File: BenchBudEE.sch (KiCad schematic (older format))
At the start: 0 parts

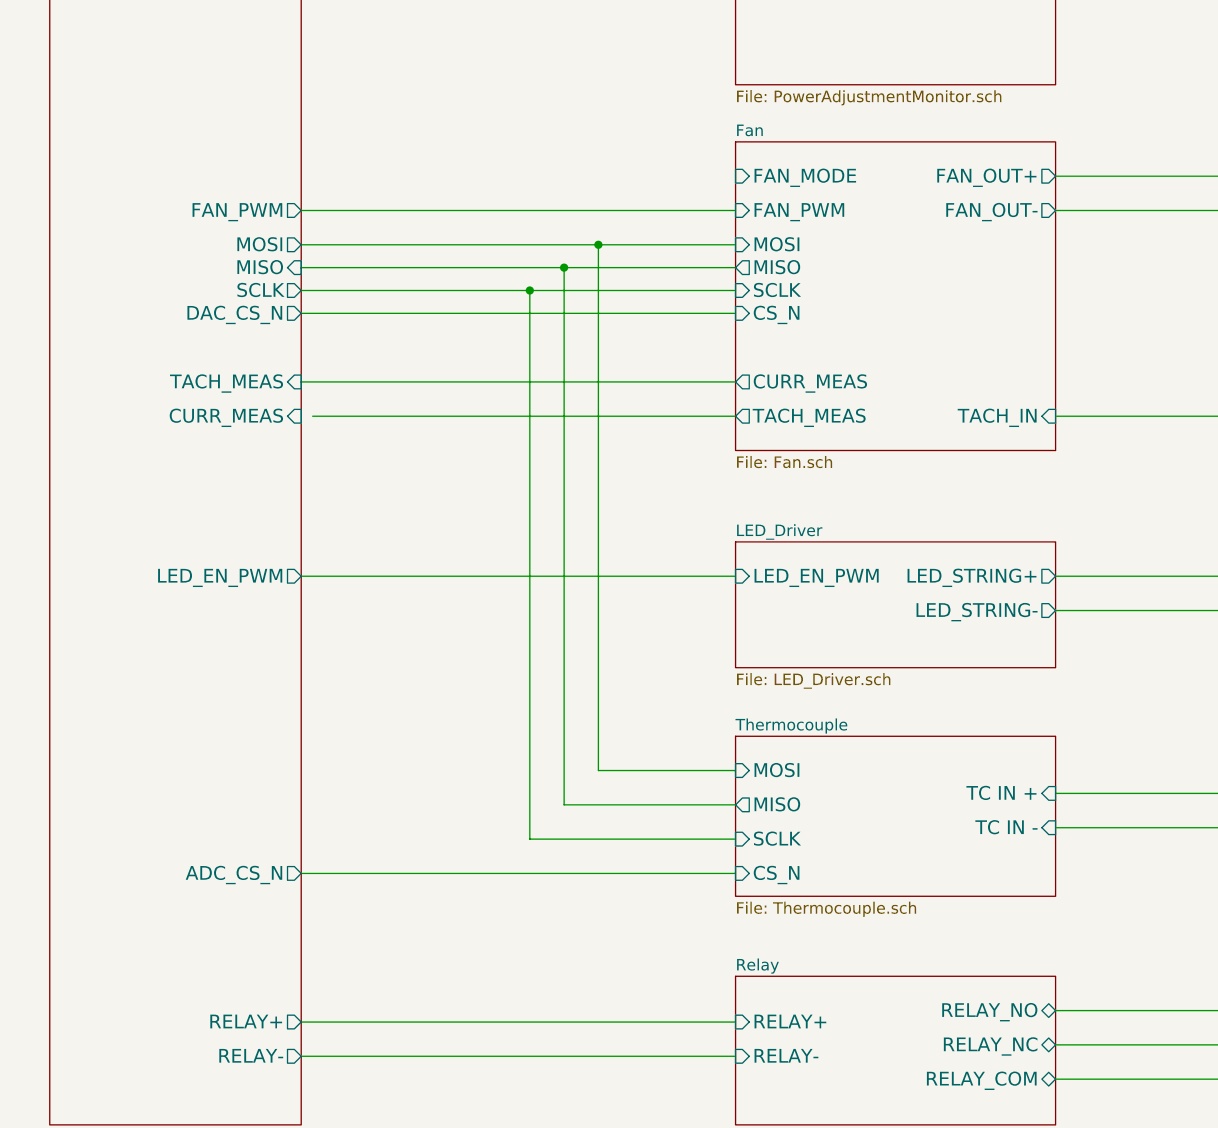
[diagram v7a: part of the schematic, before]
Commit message: worked on associating parts
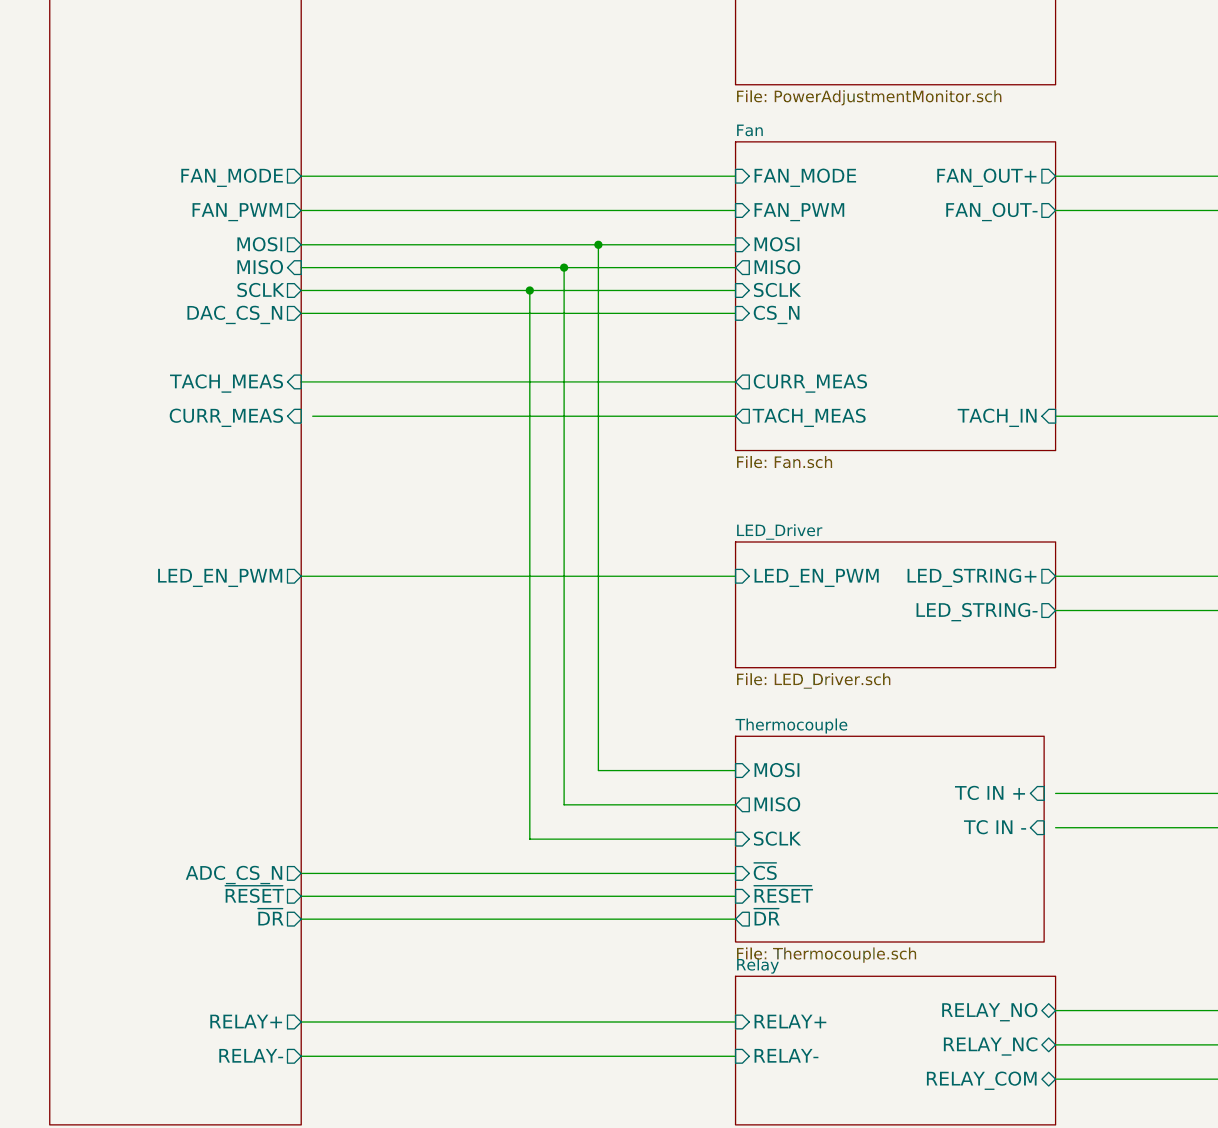
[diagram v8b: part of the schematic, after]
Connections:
- wire segments 31 -> 34
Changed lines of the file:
@@
 Sheet 1 9
 Title ""
-Date "20 feb 2014"
+Date "23 feb 2014"
 Rev ""
 Comp ""
@@
 $EndDescr
 $Sheet
-S 6250 4950 1400 700
+S 6250 4950 1350 900
 U 52EEE626
 F0 "Thermocouple" 50
 F1 "Thermocouple.sch" 50
-F2 "TC IN +" I R 7650 5200 60
-F3 "TC IN -" I R 7650 5350 60
+F2 "TC IN +" I R 7600 5200 60
+F3 "TC IN -" I R 7600 5350 60
 F4 "MOSI" I L 6250 5100 60
 F5 "MISO" O L 6250 5250 60
 F6 "SCLK" I L 6250 5400 60
-F7 "CS_N" I L 6250 5550 60
+F7 "~CS" I L 6250 5550 60
+F8 "~DR" O L 6250 5750 60
+F9 "~RESET" I L 6250 5650 60
 $EndSheet
 $Sheet
@@
 F13 "ADC_CS_N" O R 4350 5550 60
 F14 "FAN_PWM" O R 4350 2650 60
+F15 "FAN_MODE" O R 4350 2500 60
+F16 "~RESET" O R 4350 5650 60
+F17 "~DR" O R 4350 5750 60
 $EndSheet
+Wire Wire Line
+	4350 5650 6250 5650
+Wire Wire Line
+	4350 5750 6250 5750
+Wire Wire Line
+	4350 2500 6250 2500
 $EndSCHEMATC
